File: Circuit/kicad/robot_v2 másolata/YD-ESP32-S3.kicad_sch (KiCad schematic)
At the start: 18 parts, among them Q1 SS8050-G, Q2 SS8050-G, U15 CH343P, U8 ESP32-S3-WROOM-2

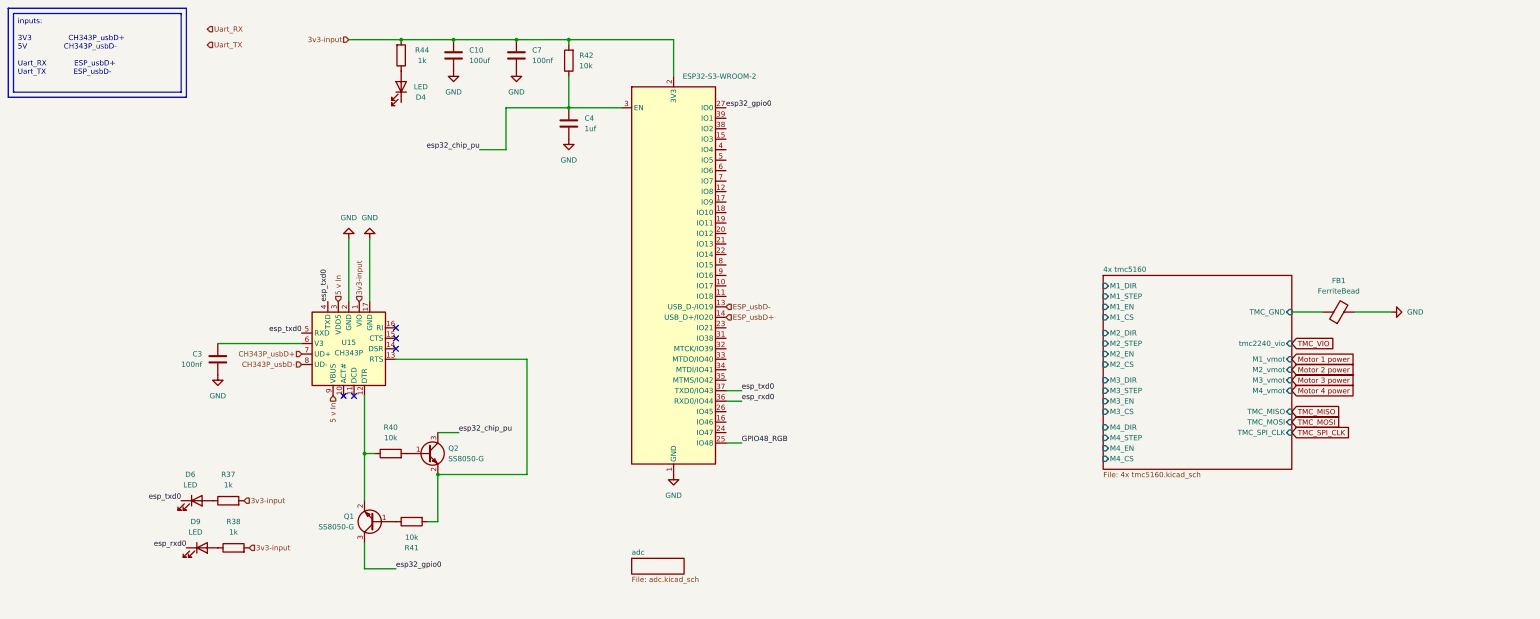
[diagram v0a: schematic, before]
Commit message: kicad i2c schematic updated: gyto i2c bugfixes, +add new datasheets
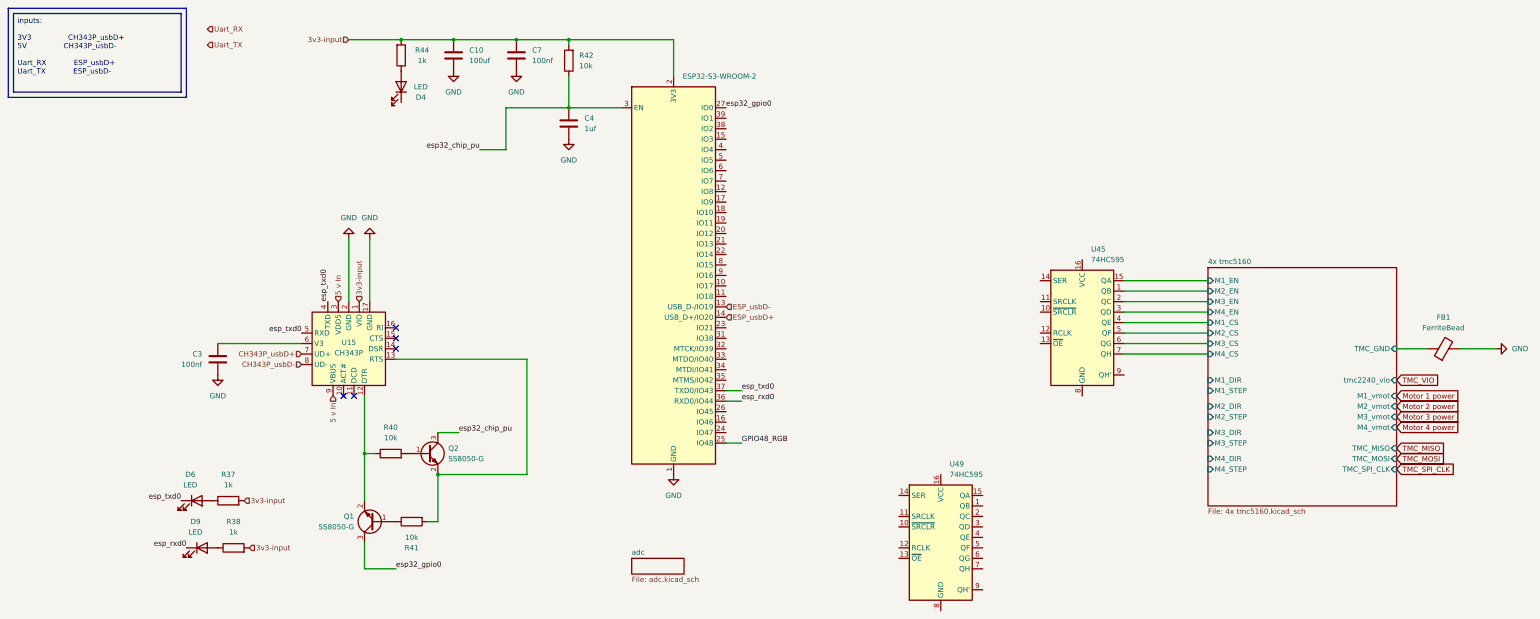
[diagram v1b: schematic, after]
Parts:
- added U45, U49: 74HC595, symbol 74xx:74HC595
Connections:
- net 4x tmc5160/M1_CS: now also U45.4 (QE)
- net 4x tmc5160/M1_EN: now also U45.15 (QA)
- net 4x tmc5160/M2_CS: now also U45.5 (QF)
- net 4x tmc5160/M2_EN: now also U45.1 (QB)
- net 4x tmc5160/M3_CS: now also U45.6 (QG)
- net 4x tmc5160/M3_EN: now also U45.2 (QC)
- net 4x tmc5160/M4_CS: now also U45.7 (QH)
- net 4x tmc5160/M4_EN: now also U45.3 (QD)
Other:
- moved on the sheet: FB1
